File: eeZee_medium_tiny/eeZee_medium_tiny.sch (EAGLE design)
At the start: 11 parts, among them IC1 TINY24/44/84, J2 avrisp, Q1 16MHz

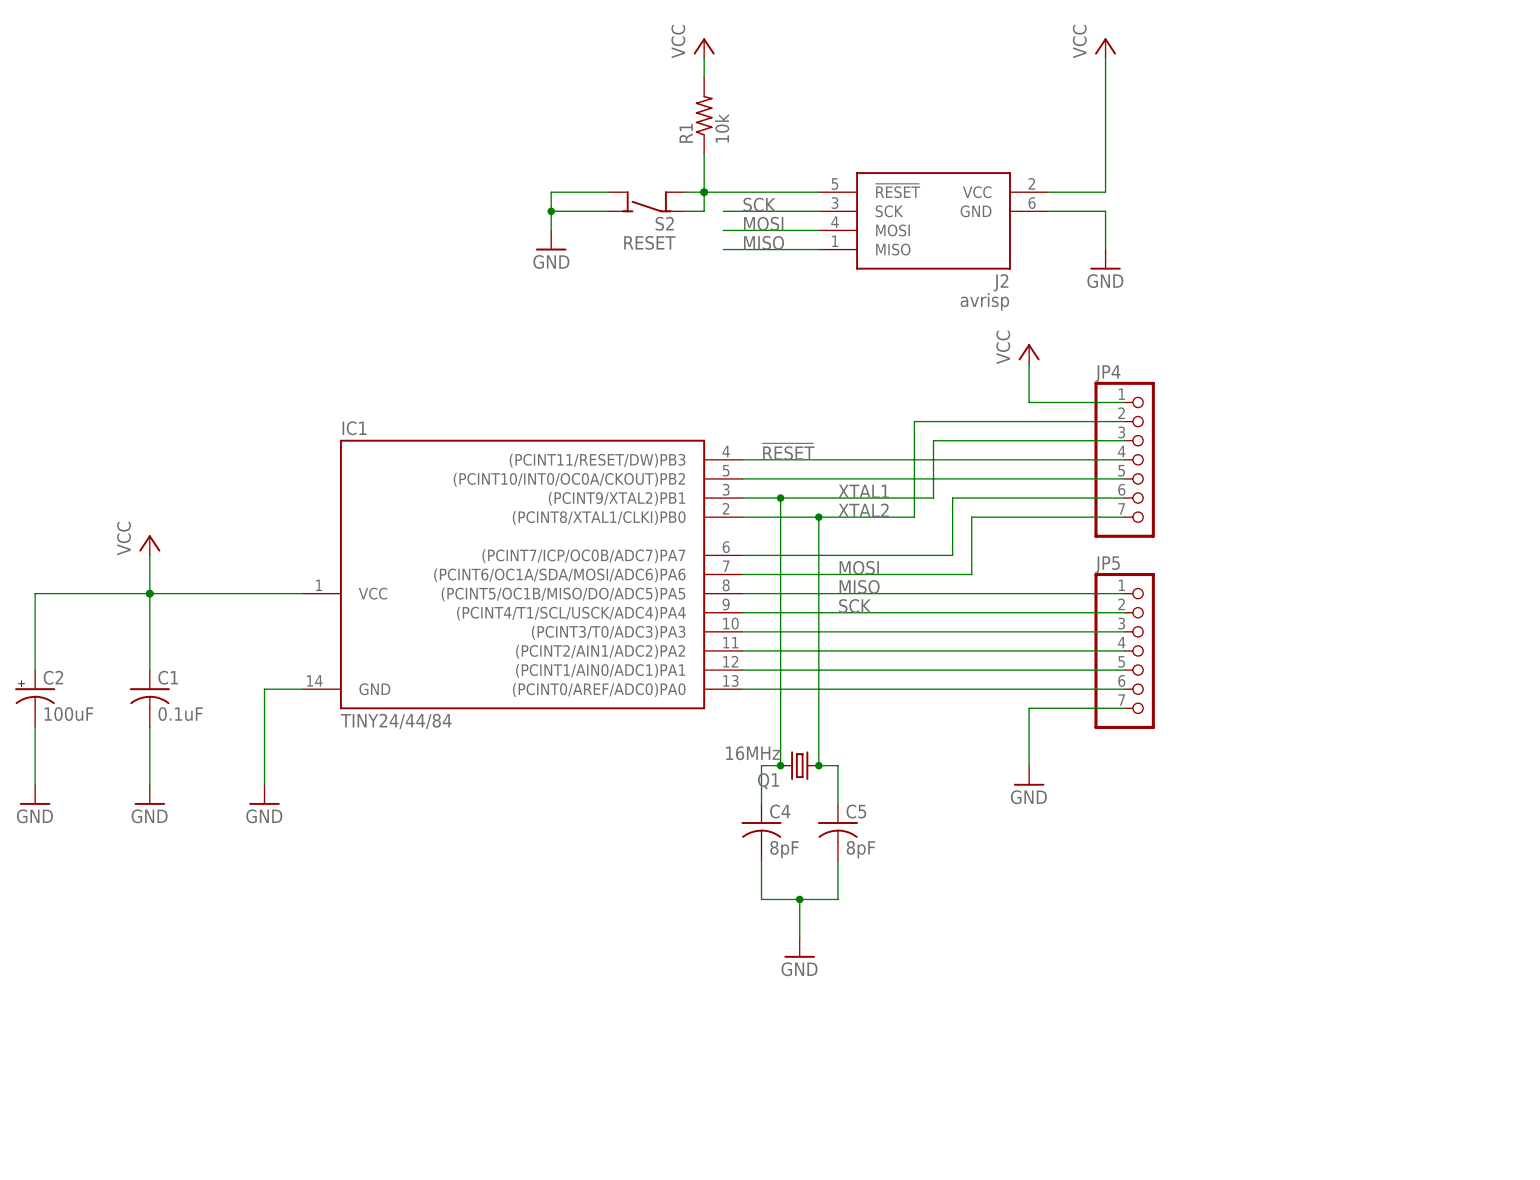
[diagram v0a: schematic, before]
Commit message: Rev 0.2 as ordered, mitered corners, flipped tantalum and added polarity silk screen, changed location of caps/crystals for easier assembly, shrunk board size.
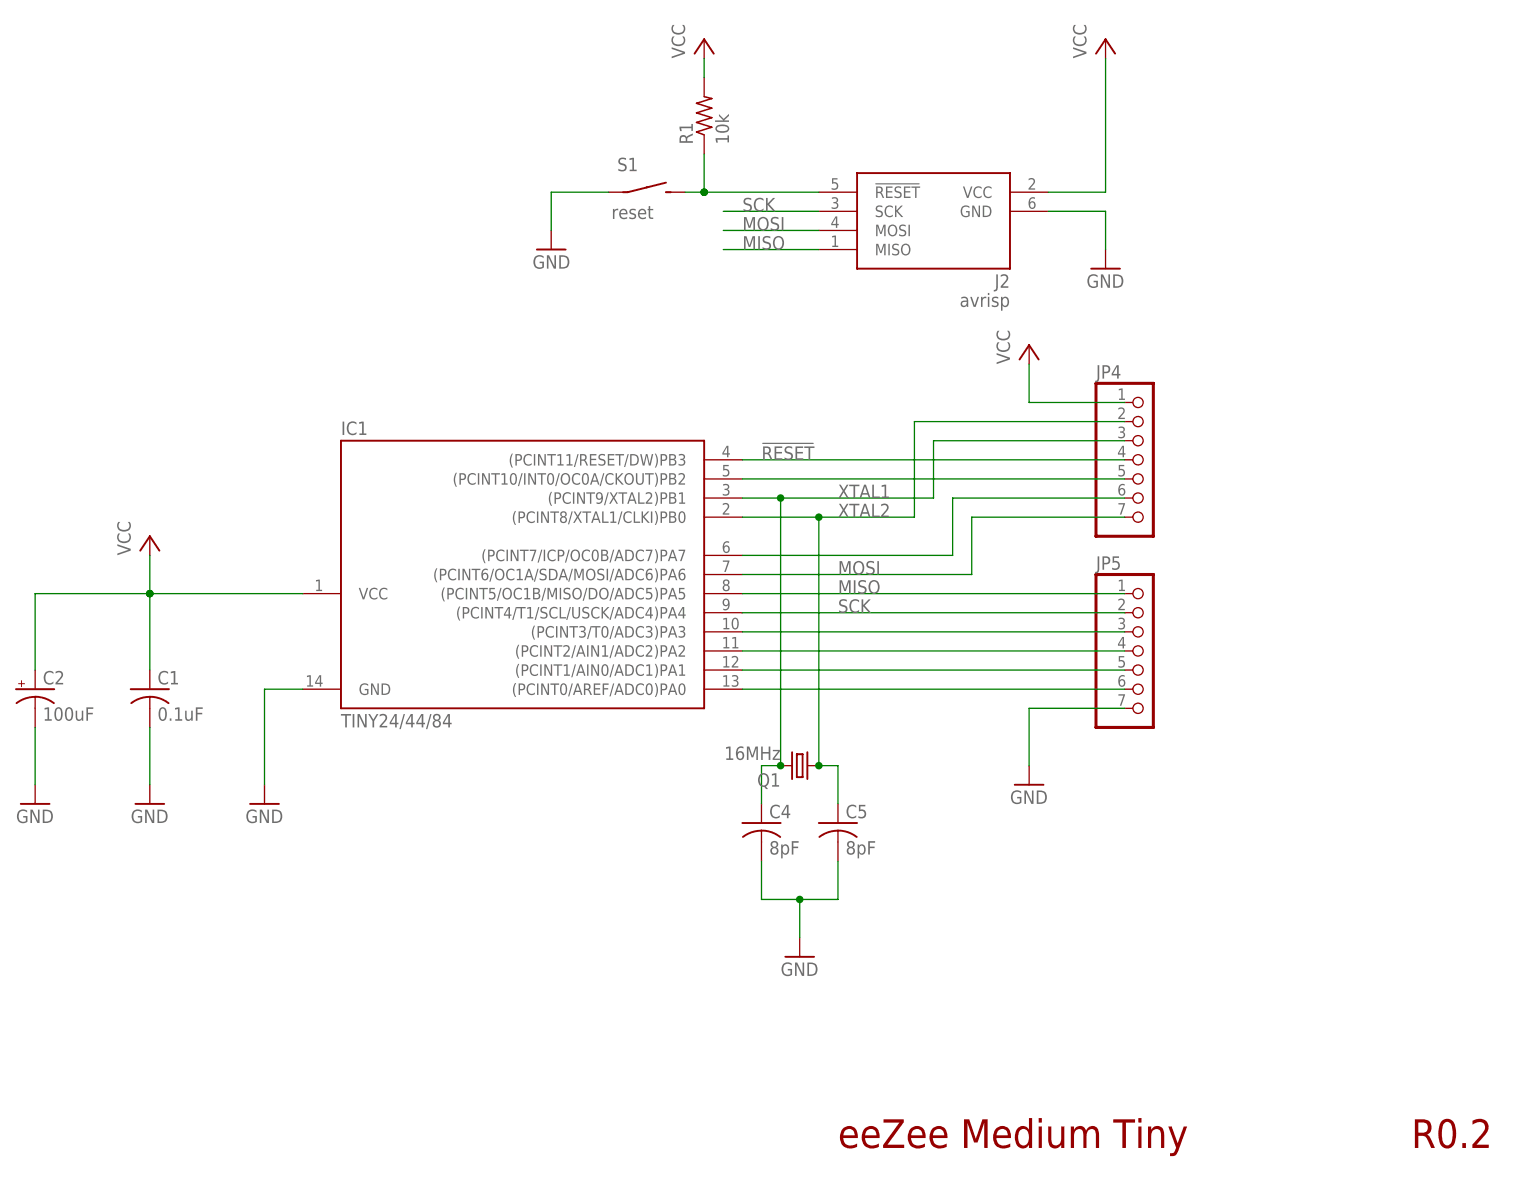
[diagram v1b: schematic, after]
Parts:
- removed S2: RESET, mes_electromech:SPST4
- added S1: reset, mes_electromech:SPST_TAC_RECT1
- C2: device rcl:CPOL-USSMCB -> mes_rcl:CAP_POL_SMC_B
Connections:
- net !RESET: now also S1.S; no longer S2.COM@1, S2.COM@2
- net GND: now also S1.P; no longer S2.NO@1, S2.NO@2
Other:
- note added: "R0.2"
- note added: "eeZee Medium Tiny"
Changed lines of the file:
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@@
 <?xml version="1.0" encoding="utf-8"?>
 <!DOCTYPE eagle SYSTEM "eagle.dtd">
-<eagle version="6.3">
+<eagle version="6.4">
 <drawing>
 <settings>
@@
 </part>
 <part name="J2" library="ads4" deviceset="AVRISP6" device="" value="avrisp"/>
-<part name="S2" library="mes_electromech" deviceset="SPST4" device="" value="RESET"/>
 <part name="P+4" library="supply1" deviceset="VCC" device=""/>
 <part name="FRAME1" library="mes" deviceset="LETTER_L" device=""/>
 <part name="GND5" library="supply1" deviceset="GND" device=""/>
 <part name="GND6" library="supply1" deviceset="GND" device=""/>
-<part name="C2" library="rcl" deviceset="CPOL-US" device="SMCB" value="100uF">
+<part name="C2" library="mes_rcl" deviceset="CAP_POL" device="_SMC_B" value="100uF">
 <attribute name="BOM" value="EXCLUDE"/>
 <attribute name="PARTNO" value="MCTT21X106M6R3CT"/>
@@
 <part name="JP5" library="pinhead-2" deviceset="PINHD-1X07" device="_2.54-S"/>
 <part name="GND4" library="supply1" deviceset="GND" device=""/>
+<part name="S1" library="mes_electromech" deviceset="SPST" device="_TAC_RECT1" value="reset"/>
 </parts>
 <sheets>
 <sheet>
 <plain>
+<text x="154.94" y="22.86" size="3.81" layer="94">eeZee Medium Tiny</text>
+<text x="231.14" y="22.86" size="3.81" layer="94">R0.2</text>
 </plain>
 <instances>
@@
 </instance>
 <instance part="J2" gate="A" x="167.64" y="142.24" rot="MR0"/>
-<instance part="S2" gate="G$1" x="129.54" y="147.32" rot="MR0"/>
 <instance part="P+4" gate="VCC" x="180.34" y="129.54"/>
 <instance part="FRAME1" gate="G$1" x="248.92" y="185.42" rot="R180"/>
-<instance part="FRAME1" gate="G$2" x="248.92" y="27.94" rot="R180"/>
+<instance part="FRAME1" gate="G$2" x="147.32" y="2.54"/>
 <instance part="GND5" gate="1" x="63.5" y="68.58"/>
 <instance part="GND6" gate="1" x="48.26" y="68.58"/>
@@
 <instance part="JP5" gate="A" x="195.58" y="88.9"/>
 <instance part="GND4" gate="1" x="180.34" y="71.12"/>
+<instance part="S1" gate="G$1" x="129.54" y="149.86"/>
 </instances>
 <busses>
@@
 </segment>
 <segment>
-<wire x1="116.84" y1="144.78" x2="116.84" y2="147.32" width="0.1524" layer="91"/>
 <pinref part="GND3" gate="1" pin="GND"/>
-<pinref part="S2" gate="G$1" pin="NO@1"/>
-<pinref part="S2" gate="G$1" pin="NO@2"/>
-<wire x1="116.84" y1="147.32" x2="124.46" y2="147.32" width="0.1524" layer="91"/>
 <wire x1="124.46" y1="149.86" x2="116.84" y2="149.86" width="0.1524" layer="91"/>
-<wire x1="116.84" y1="149.86" x2="116.84" y2="147.32" width="0.1524" layer="91"/>
-<junction x="116.84" y="147.32"/>
+<wire x1="116.84" y1="149.86" x2="116.84" y2="144.78" width="0.1524" layer="91"/>
+<pinref part="S1" gate="G$1" pin="P"/>
 </segment>
 <segment>
@@
 <junction x="137.16" y="149.86"/>
 <pinref part="R1" gate="G$1" pin="1"/>
-<wire x1="134.62" y1="147.32" x2="137.16" y2="147.32" width="0.1524" layer="91"/>
 <pinref part="J2" gate="A" pin="!RESET"/>
-<pinref part="S2" gate="G$1" pin="COM@1"/>
-<pinref part="S2" gate="G$1" pin="COM@2"/>
 <wire x1="134.62" y1="149.86" x2="137.16" y2="149.86" width="0.1524" layer="91"/>
 <junction x="137.16" y="149.86"/>
-<wire x1="137.16" y1="147.32" x2="137.16" y2="149.86" width="0.1524" layer="91"/>
-</segment>
-<segment>
+<pinref part="S1" gate="G$1" pin="S"/>
+</segment>
+<segment>
